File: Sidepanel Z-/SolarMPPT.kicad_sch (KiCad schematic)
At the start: 19 parts, among them U11 INA180A4

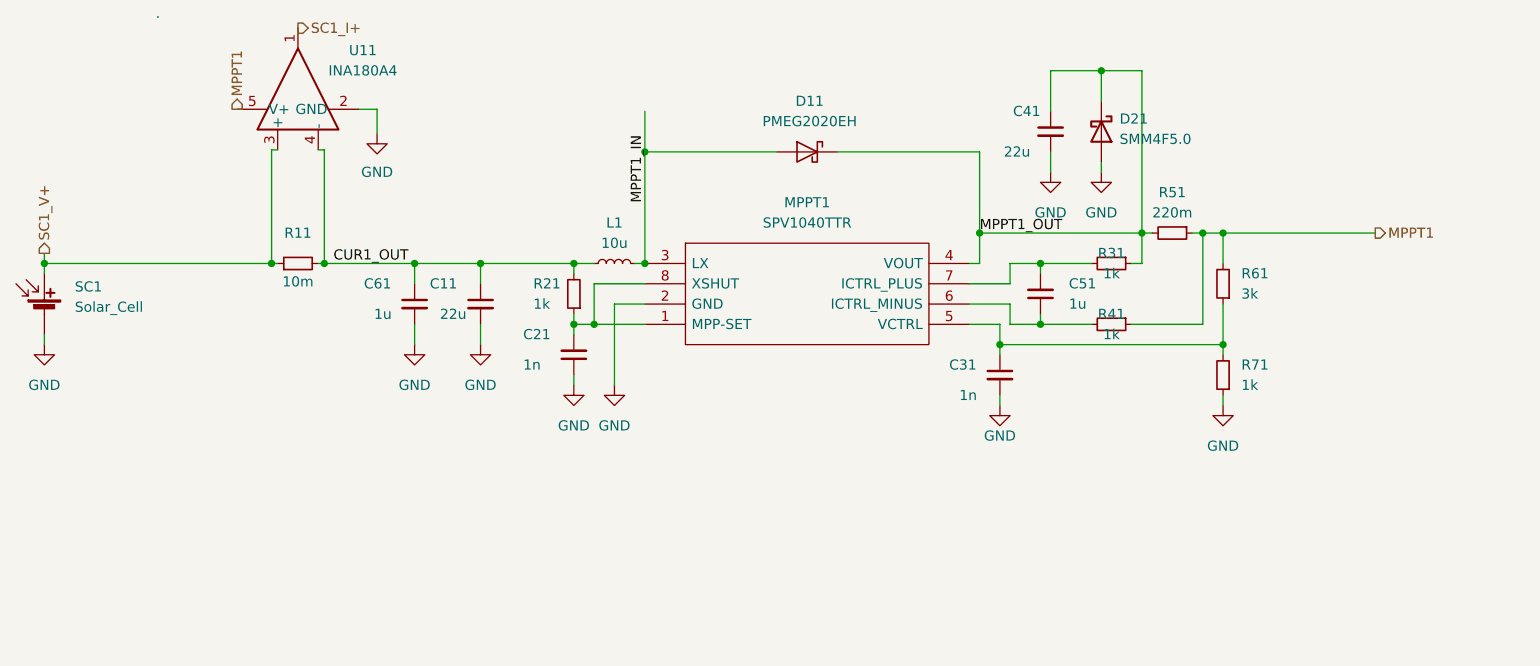
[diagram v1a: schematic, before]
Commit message: mirror the pinout of the connector on the Z- panel, split output capacitor in two capacitors
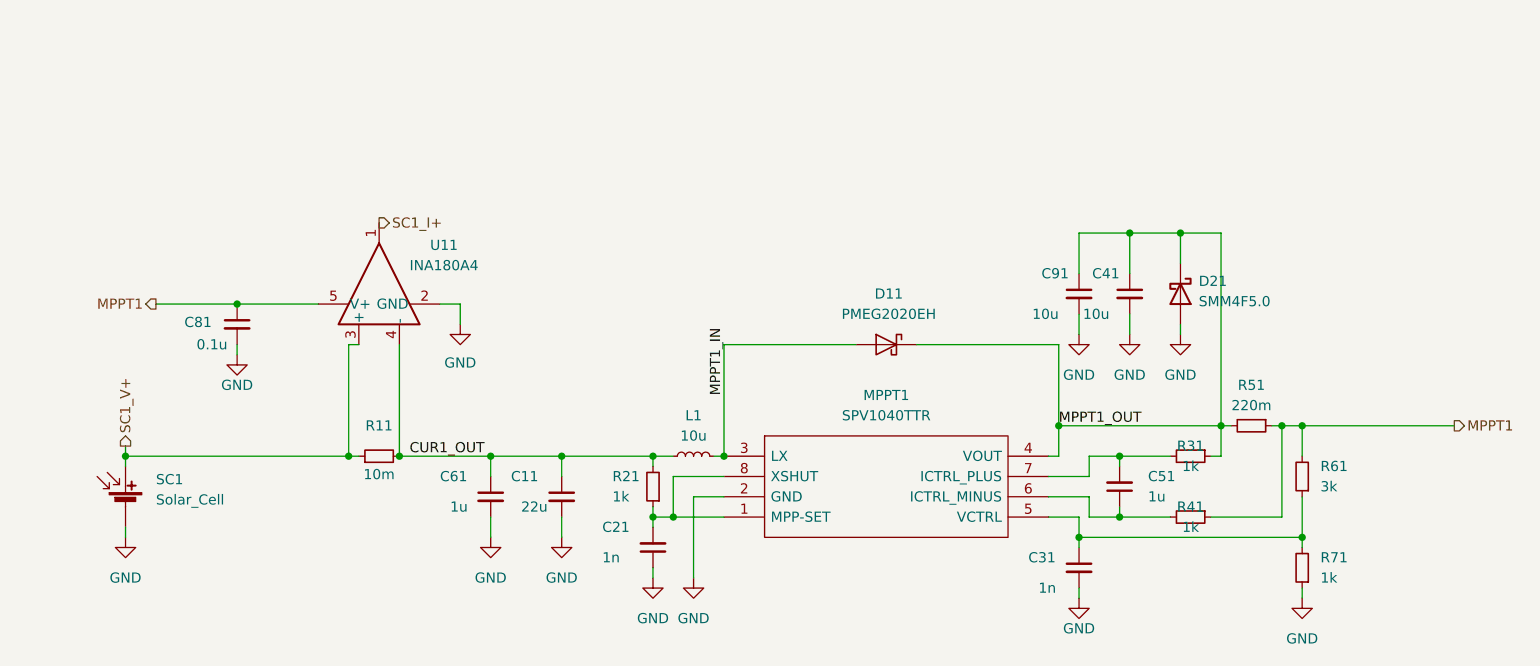
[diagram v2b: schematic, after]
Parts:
- added C81: 0.1u, Capacitor_SMD:C_0603_1608Metric, symbol Device:C_Small
- added C91: 10u, Capacitor_SMD:C_0805_2012Metric, symbol Device:C_Small
- C41: value 22u -> 10u
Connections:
- net GND: now also C81.2, C91.2
- net MPPT1: now also C81.1
- net MPPT1_OUT: now also C91.1
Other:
- moved on the sheet: C11, C21, C31, C41, C51, C61, D11, D21, L1, MPPT1, R11, R21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
